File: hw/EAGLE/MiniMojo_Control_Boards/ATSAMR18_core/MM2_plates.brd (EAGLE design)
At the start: 39.6 x 29.5 mm, 54 parts, among them J1 CORTEX_DEBUGSMD, Q1 MOSFET-NCHANNEL2N7002PW, U1 3.3V, U2 EM406, U3 Value

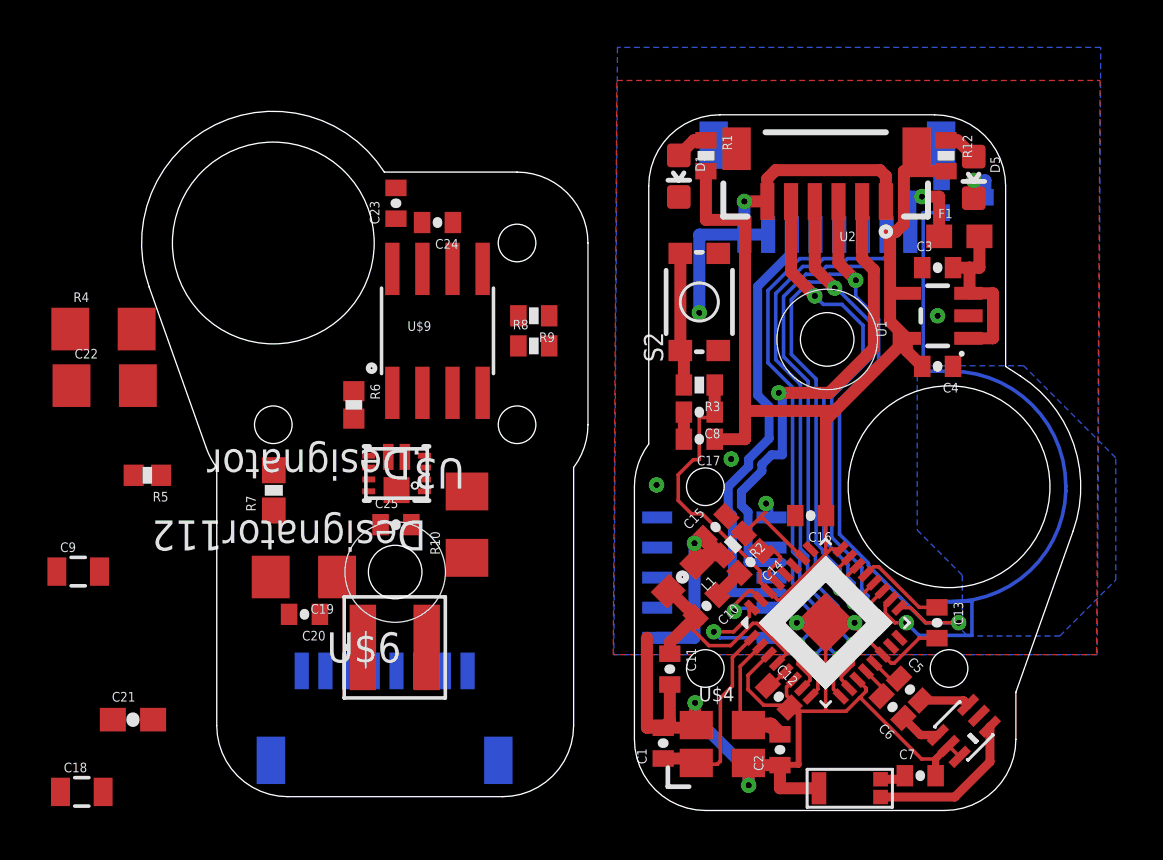
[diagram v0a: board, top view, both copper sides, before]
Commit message: added TPS61089 w/ Tiny841
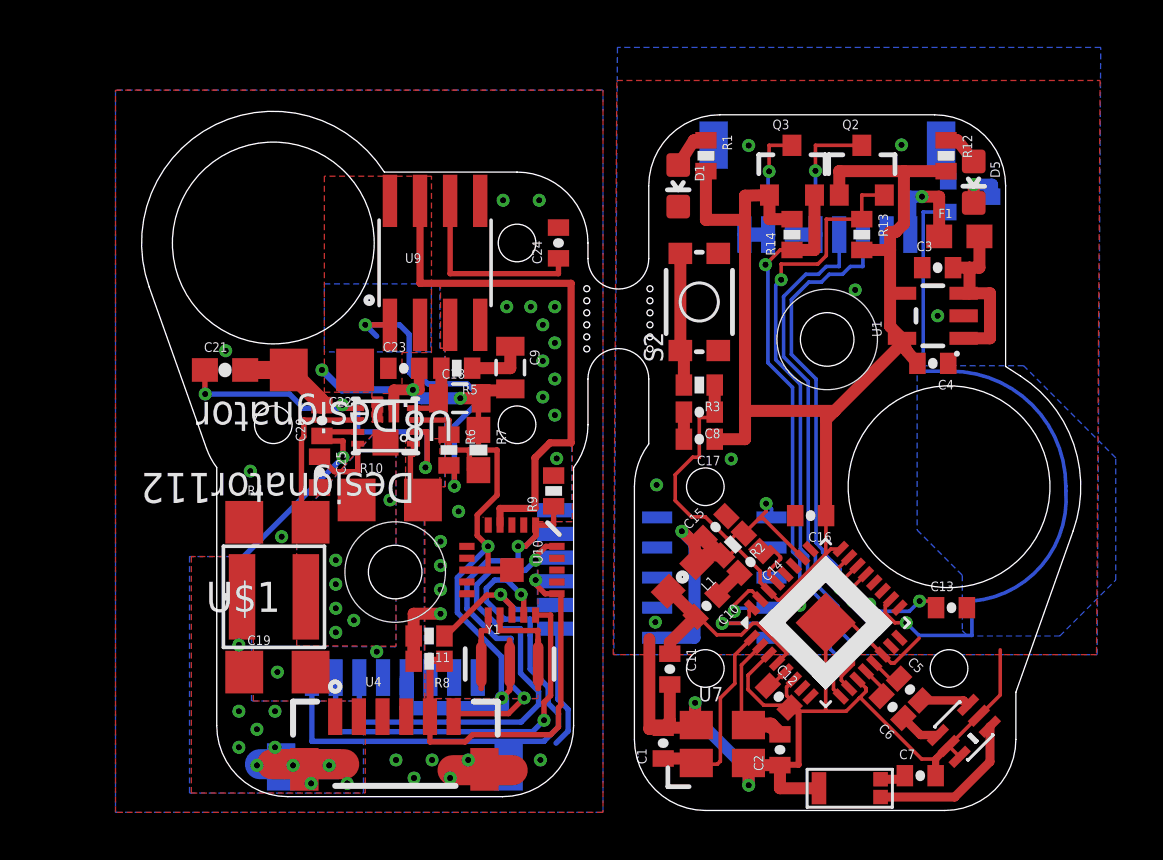
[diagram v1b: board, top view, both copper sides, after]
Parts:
- removed U$10: EB-85ASMD, SparkFun-Connectors:EB-85A
- removed U$6: XAL4020-122MEB, TPS61089RNRR_4.8V:XAL4020
- removed U$9: ACS712, SparkFun-AnalogIC:SO08
- removed U3: Value, TPS61089RNRR_4.8V:RNR0011A
- added J3: (no value), CSL_Components:1X06-1MM
- added Q2, Q3: MOSFET-NCHANNELAO3404A, SparkFun-DiscreteSemi:SOT23-3
- added R11, R13, R14: 10k, SparkFun-Passives:0402-RES
- added U10: ATTINY84ATTINY84-20MU, SparkFun-DigitalIC:QFN20
- added U11: EB-85ASMD, SparkFun-Connectors:EB-85A
- added U4: EM406, SparkFun-Connectors:EM406
- added U8: Value, TPS61089RNRR_4.8V:RNR0011A
- added U9: ACS712, SparkFun-AnalogIC:SO08
- added Y1: 16MHZ, SparkFun-FreqCtrl:RESONATOR-SMD
- C18: value (none) -> 62 pF
- C19, C22: value (none) -> 47 uF
- C20, C25: value (none) -> 100 nF
- C21: value (none) -> 2.2 uF
- C9: value (none) -> 1.2 nF
- R10: value (none) -> 523k
- R4: value (none) -> 143k
- R5: value (none) -> 22.6k; device SparkFun-Resistors:0402-RES -> SparkFun-Passives:0402-RES
- R6: value (none) -> 243k; device SparkFun-Resistors:0402-RES -> SparkFun-Passives:0402-RES
- R7: value (none) -> 82k
- R8: value 2k -> 10k
- U$1: value ATSAMR21E18A-MUT -> XAL4020-122MEB; device atmel-samr21:QFN32 -> TPS61089RNRR_4.8V:XAL4020
- U2: value EM406 -> ATSAMR21E18A-MUT; device SparkFun-Connectors:EM406 -> atmel-samr21:QFN32
- moved U$1 23.3 mm to (9.73, 10.6), turned to 0 degrees
- moved C18 23.0 mm to (17.6, 19.0)
- moved C9 20.2 mm to (19.7, 20.3), turned to 270 degrees
- moved U2 18.0 mm to (33.0, 9.53), turned to 45 degrees
- moved C21 15.3 mm to (7.67, 20.2)
- moved R8 14.0 mm to (16.3, 7.90), turned to 180 degrees
- moved R5 13.8 mm to (17.4, 20.3)
- moved R4 11.0 mm to (9.88, 13.8)
- moved C22 9.19 mm to (11.8, 20.2), turned to 180 degrees
- moved R7 8.80 mm to (18.4, 16.8), turned to 270 degrees
- moved C20 8.21 mm to (11.8, 18.1), turned to 90 degrees
- moved R9 7.44 mm to (21.5, 15.1), turned to 90 degrees
- moved C23 6.97 mm to (15.2, 20.3), turned to 0 degrees
- moved C24 5.18 mm to (21.7, 25.6), turned to 90 degrees
- moved R6 4.44 mm to (17.1, 16.8)
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- renumbered U$2 to U6, U$3 to U5, U$4 to U7, U$5 to U12
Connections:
- removed net CURRENT_SIG1: U$1.7, U12.3
- removed net CURRENT_SIG2: U$1.8, U2.2
- removed net MOTSIG3: U$10.3
- removed net N$12: U6.2
- removed net N$17: R8.1, U$9.7
- removed net SERVOB1: U$1.20, U2.5
- removed net SERVOB2: U$1.19, U2.4
- removed net SERVOHIP: U$1.17, U2.3
- removed net SERVOT1: U$1.9, U12.4
- removed net SERVOT2: U$1.10, U12.5
- new net MOTSIG0: U10.14, U11.8
- new net N$4: U10.12, Y1.3
- new net N$5: U10.11, Y1.1
- new net SCL: J3.2, R9.1, U10.1, U4.6
- new net SCL_HV: Q2.3, U12.3, U12.4
- new net SCL_LV: Q2.2, R13.1, U2.10
- new net SDA: J3.4, R8.1, U10.16, U4.5
- new net SDA_HV: Q3.3, U12.1, U12.2
- new net SDA_LV: Q3.2, R14.1, U2.9
- net 3.3V: now also Q2.1, Q3.1, R13.2, R14.2, U2.24, U2.30; no longer U$1.24, U$1.30
- net AVDD: now also U2.5; no longer U$1.5
- net BLINK: now also U2.18; no longer U$1.18
- net CURSENSE: now also U10.4, U9.7; no longer R8.2, R9.1, U$10.4
- net DVDD: now also U2.21; no longer U$1.21
- net GND: now also J3.6, U10.8, U11.4, U11.5, U12.7, U2.11, U2.14, U2.3, U2.33, U4.3, U4.4, U6.2, U8.5, U9.5, Y1.2; no longer R9.2, U$1.11, U$1.14, U$1.3, U$1.33, U$1.6, U$10.5, U$10.6, U$9.5, U12.1, U12.2, U2.1, U3.5
- net MOTSIG1: now also U10.15, U11.7; no longer U$10.2
- net MOTSIG2: now also J3.3, U10.20, U11.6; no longer U$10.1
- net N$15: now also U8.4; no longer U3.4
- net N$16: now also U9.6; no longer U$9.6
- net N$19: now also U8.2, U8.7; no longer U3.2, U3.7
- net N$27: now also U8.10; no longer U3.10
- net N$28: now also U$1.2, U8.11; no longer U$6.2, U3.11
- net N$29: now also U8.1; no longer U3.1
- net N$3: now also U8.8; no longer U3.8
- net N$31: now also U8.3; no longer U3.3
- net PA24/USBDM: now also U12.6, U2.22; no longer U$1.22, U12.7
- net PA25/USBDP: now also U12.5, U2.23; no longer U$1.23, U12.6
- net RESET: now also J3.5, R11.1, U10.13, U2.26; no longer U$1.26
- net RFN: now also U2.13; no longer U$1.13
- net RFP: now also U2.12; no longer U$1.12
- net SWCLK: now also U2.31; no longer U$1.31
- net SWDIO: now also U2.32; no longer U$1.32
- net VDDANA: now also U2.4; no longer U$1.4
- net VDDCORE: now also U2.29; no longer U$1.29
- net VMOT: now also J3.1, R11.2, R8.2, R9.2, U10.9, U11.1, U11.2, U11.3, U9.3, U9.4; no longer U$9.3, U$9.4
- net V_BATT: now also U$1.1, U4.1, U4.2, U8.9; no longer U$10.7, U$10.8, U$6.1, U3.9
- net V_MOT_UNSENSE: now also U8.6, U9.1, U9.2, U9.8; no longer U$9.1, U$9.2, U$9.8, U3.6
- net XIN: now also U2.1; no longer U$1.1
- net XOUT: now also U2.2; no longer U$1.2
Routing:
- net GND: track 65.6 -> 102.8 mm, vias 9 -> 30
- net CURRENT_SIG2: track 29.4 -> 0.00 mm, vias 2 -> 0
- net SCL_LV: track 0.00 -> 26.8 mm, vias 0 -> 2
- net SERVOHIP: track 24.8 -> 0.00 mm, vias 2 -> 0
- net SDA_LV: track 0.00 -> 24.4 mm, vias 0 -> 2
- net CURRENT_SIG1: track 24.2 -> 0.00 mm, vias 1 -> 0
- net MOTSIG0: track 0.00 -> 23.9 mm, vias 0 -> 1
- net SERVOT2: track 22.7 -> 0.00 mm, vias 1 -> 0
- net CURSENSE: track 0.00 -> 22.7 mm
- net SERVOT1: track 22.4 -> 0.00 mm, vias 1 -> 0
- net SERVOB2: track 22.0 -> 0.00 mm, vias 2 -> 0
- net MOTSIG2: track 0.00 -> 21.4 mm, vias 0 -> 1
- net V_BATT: track 0.00 -> 21.3 mm, vias 0 -> 12
- net SERVOB1: track 21.0 -> 0.00 mm, vias 2 -> 0
- net SDA: track 0.00 -> 17.8 mm, vias 0 -> 1
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- added copper zone on layer 1, net N$28
- added copper zone on layer 16, net N$28
- added copper zone on layer 1, net N$29
- added copper zone on layer 1, net VMOT
- added copper zone on layer 16, net VMOT
- added copper zone on layer 1, net V_BATT
- added copper zone on layer 16, net V_BATT
- added copper zone on layer 1, net V_MOT_UNSENSE
- added copper zone on layer 16, net V_MOT_UNSENSE
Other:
- outline, holes or cut-outs redrawn
- board text added: "CSL 2016"
- board text added: "MINI MOJO"
